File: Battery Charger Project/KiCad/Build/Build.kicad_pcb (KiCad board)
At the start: 2 copper layers, 135 x 107 mm, 63 parts, among them J1 726386-2, J10 726386-2, J11 726386-2, J2 726386-2, J3 726386-2, J4 Screw_Terminal_01x02, J5 726386-2, J6 726386-2, J7 726386-2, J8 Screw_Terminal_01x05, J9 726386-2, T1 Transformer_SP_1S, U1 LAUNCHXL-F28379D, U2 LNK6773K-TL, U3 MCS1801GS-25-P, U4 L4941BV

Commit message: More updates on PCB design
I forgot to push my changes for the last week, but I layed out the components and began routing traces and copper pours.
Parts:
- removed C11, C13, C14, C15, C16, C18, C19: C_Small, Capacitor_SMD:C_0805_2012Metric_Pad1.18x1.45mm_HandSolder
- removed C12: UHE1E102MHD6TO, footprints_C10:CAP_UAQ_12P5X20_NCH
- removed C17, C21: 0.1uF, Capacitor_SMD:C_0805_2012Metric_Pad1.18x1.45mm_HandSolder
- removed C20: ~, footprints_C20:CAP_WCAP-ATG5_05.0X11.0_WRE
- removed D2, D5: D_Zener, Diode_SMD:D_SMA-SMB_Universal_Handsoldering
- removed D3: US1M, Diode_SMD:D_SMA
- removed D4: STPS2H100U, footprints_SCHOTTKYDIODE:SMB_STM
- removed J10, J7, J9: 726386-2, KiCad:726386-2
- removed J11: 726386-2, Library:726386-2
- removed J8: Screw_Terminal_01x05, TerminalBlock_Phoenix:TerminalBlock_Phoenix_MPT-0,5-5-2.54_1x05_P2.54mm_Horizontal
- removed R10, R14, R15, R16, R17, R9: R_Small_US, Resistor_SMD:R_2010_5025Metric
- removed R11, R12, R19: R_Small_US, Resistor_SMD:R_0805_2012Metric
- removed R13: R_Small_US, Resistor_SMD:R_0805_2012Metric_Pad1.20x1.40mm_HandSolder
- removed R18, R20, R7: R_Small_US, Resistor_SMD:R_1206_3216Metric
- removed R8: R_Small_US, Resistor_SMD:R_1206_3216Metric_Pad1.30x1.75mm_HandSolder
- removed T1: Transformer_SP_1S, Library:Transformer_cust_v1
- removed U3: MCS1801GS-25-P, KiCadCS:SOIC127P600X175-8N
- removed U4: L4941BV, L4941BV:TO-220_STM
- C1: value UVR2G220MHD -> C_Small; footprint footprints_C1:CAP_UAQ_16X25_NCH -> Capacitor_SMD:C_0805_2012Metric_Pad1.18x1.45mm_HandSolder; moved to B.Cu
- C10, C3: value C_Small -> ~; footprint Capacitor_SMD:C_1206_3216Metric -> LGW2D561MELA30:CAP_A30_NCH; moved to F.Cu
- C2: footprint Capacitor_SMD:C_1206_3216Metric -> Capacitor_SMD:C_0805_2012Metric_Pad1.18x1.45mm_HandSolder; moved to B.Cu
- C4: value B32673P6225K000 -> C_Small; footprint KiCad_B326:B32673P__26.5_x_12_ -> Capacitor_SMD:C_0805_2012Metric_Pad1.18x1.45mm_HandSolder; moved to B.Cu
- C5, C6: moved to B.Cu
- C7: footprint footprints:CAP_C45_NCH -> EEU-FR1H100:CAP_PAN_5X11_PAN
- C8: value C_Small -> ~; footprint Capacitor_SMD:C_0805_2012Metric_Pad1.18x1.45mm_HandSolder -> LGW2D561MELA30:CAP_A30_NCH
- C9: value C_Small -> ~; footprint Capacitor_SMD:C_0805_2012Metric_Pad1.18x1.45mm_HandSolder -> LGW2D561MELA30:CAP_A30_NCH; moved to F.Cu
- D1: value US1M -> DNA40U2200GU; footprint Diode_SMD:D_SMA -> DPF30U200FC:DPF30U200FC; moved to F.Cu
- J1: value 726386-2 -> Screw_Terminal_01x03; footprint KiCad:726386-2 -> 284391-3:CONN3_284391-3_TEC
- J2: value 726386-2 -> Screw_Terminal_01x02; footprint KiCad:726386-2 -> 284391-2:CONN2_284391-2_TEC
- J3: value 726386-2 -> Screw_Terminal_01x03; footprint KiCad:726386-2 -> 277-1578-ND:CONN_1935174_PXC
- J4: value Screw_Terminal_01x02 -> 726386-2; footprint TerminalBlock:TerminalBlock_bornier-2_P5.08mm -> 284391-2:CONN2_284391-2_TEC
- J5, J6: footprint KiCad:726386-2 -> 284391-2:CONN2_284391-2_TEC
- L1: footprint Library:inductor_customized_v1 -> LC200-0185:LC200-0185
- R1: value R_US -> 300K; moved to B.Cu
- R2: value R_US -> 6490; moved to B.Cu
- R3: value R_US -> 36; moved to B.Cu
- R4: value R_US -> 5K; moved to B.Cu
- R5: value R_Small_US -> 680; footprint Resistor_SMD:R_1206_3216Metric -> Resistor_SMD:R_2010_5025Metric
- R6: value R_Small_US -> 680; moved to B.Cu
- U1: footprint Library:MOD_LAUNCHXL-F28379D_v2 -> LAUNCHXL-F28379D:LAUNCHXL-F28379D
- U2: value LNK6773K-TL -> TMCS1133C3A; footprint KiCad2:LNK6773KTL -> TMCS1133C5AQDVGR:TMCS1133C5AQDVGR
- moved J4 136.4 mm to (213.1, 131.4), turned to -90 degrees
- moved J3 124.3 mm to (89.9, 131.9), turned to -90 degrees
- moved D1 115.8 mm to (99.5, 134.9), turned to 180 degrees
- moved J5 114.3 mm to (213.9, 114.4), turned to 90 degrees
- moved C9 109.6 mm to (194.6, 127.7), turned to -90 degrees
- moved C4 86.2 mm to (178.3, 79.7)
- moved R5 71.4 mm to (130.6, 113.6), turned to 90 degrees
- moved R4 69.0 mm to (140.2, 113.6)
- moved C3 68.7 mm to (168.4, 127.6)
- moved U1 67.9 mm to (216.5, 31.7), turned to 180 degrees
- moved C10 67.8 mm to (142.2, 127.6), turned to -90 degrees
- moved R3 65.2 mm to (200.7, 137.5), turned to 180 degrees
- moved R1 65.0 mm to (200.7, 127.9), turned to 0 degrees
- moved R2 65.0 mm to (202.3, 132.7)
- moved C2 64.9 mm to (209.5, 53.0), turned to 90 degrees
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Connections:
- C1 pad 1: Net-(D1-K) -> PWMA
- C10 pad 1: Net-(C10-Pad1) -> VHV
- C10 pad 2: 12V -> GND
- C2 pad 1: Net-(U2-PD) -> 5V
- C3 pad 1: Net-(C3-Pad1) -> VHV
- C3 pad 2: Net-(D2-K) -> GND
- C4 pad 1: GND -> VHV_S
- C4 pad 2: Net-(C4-Pad2) -> GND
- C5 pad 1: Net-(U2-CP) -> Vo_S
- C5 pad 2: Net-(C5-Pad2) -> GND
- C6 pad 1: Net-(U2-BP) -> Io_S
- C7 pad 1: Net-(U3-IP+_1) -> Net-(U2-IN+)
- C8 pad 1: Net-(U2-CP) -> VHV
- C9 pad 1: PWMA -> VHV
- D1 pad 1: Net-(D1-K) -> VHV
- D1 pad 2: VHV -> GND
- J1 pad 1: VHV -> GND
- J1 pad 2: VHV -> PWMA
- J2 pad 1: GND -> 5V
- J3 pad 1: unconnected-(J3-Pad1) -> /A
- J3 pad 2: unconnected-(J3-Pad1) -> /B
- J4 pad 1: 12V -> VHV
- J6 pad 1: Net-(C4-Pad2) -> GND
- J6 pad 2: Net-(C4-Pad2) -> Vo
- L1 pad 2: Net-(U3-IP+_1) -> Net-(U2-IN+)
- R1 pad 2: Net-(R1-Pad2) -> VHV_S
- R2 pad 1: Net-(R1-Pad2) -> VHV_S
- R3 pad 2: VHV1 -> GND
- R4 pad 1: VHV1 -> Net-(U2-IN+)
- R4 pad 2: GND -> Vo_S
- R5 pad 1: Net-(D1-K) -> Net-(R5-Pad1)
- R5 pad 2: Net-(D2-A) -> GND
- R6 pad 1: Net-(U2-PD) -> Vo_S
- R6 pad 2: GND -> Net-(R5-Pad1)
- U1 pad J3_10: Net-(U1C-ADCINA0/ANALOGIN(DACA)) -> Io_S
- U1 pad J3_4: VHV1 -> VHV_S
- U1 pad J3_7: Board Temp -> unconnected-(U1C-ADCINC2/ANALOGIN-PadJ3_7)
- U1 pad J3_8: Vo -> Vo_S
- U1 pad J4_9: PWMB -> unconnected-(U1D-GPIO1/PWMOUT1B-PadJ4_9)
- U2 pad 1: Net-(U2-PD) -> Net-(U2-IN+)
- U2 pad 10: GND -> (no net)
- U2 pad 2: Net-(U2-FB) -> Vo
- U2 pad 3: Net-(U2-CP) -> GND
- U2 pad 4: Net-(U2-BP) -> (no net)
- U2 pad 6: Net-(D3-A) -> Io_S
- U2 pad 7: GND -> (no net)
- U2 pad 8: GND -> (no net)
- U2 pad 9: GND -> +5V
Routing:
- net GND: track 624.9 -> 3.86 mm, vias 2 -> 0
- net 5V: track 260.0 -> 0.00 mm, vias 3 -> 0
- net Vo: track 162.5 -> 0.00 mm, vias 1 -> 0
- net Ibatt: track 145.5 -> 0.00 mm
- net VHV1: track 115.5 -> 0.00 mm
- net Net-(U3-IP+_1): track 60.1 -> 0.00 mm
- net Board Temp: track 59.9 -> 0.00 mm, vias 2 -> 0
- net Net-(C4-Pad2): track 53.3 -> 0.00 mm
- net PWMA: track 52.2 -> 0.00 mm
- net 12V: track 47.9 -> 0.00 mm
- net PWMB: track 46.6 -> 0.00 mm
- net Net-(U2-BP): track 41.8 -> 0.00 mm, vias 2 -> 0
- net Net-(U2-FB): track 35.3 -> 0.00 mm, vias 2 -> 0
- net VHV: track 37.2 -> 3.88 mm
- net Net-(J5-Pad1): track 26.8 -> 0.00 mm
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- added copper zone on B.Cu, net /A
- added copper zone on F.Cu, net /A
- added copper zone on B.Cu, net /B
- added copper zone on F.Cu, net /B
- added copper zone on B.Cu, net /C
- added copper zone on F.Cu, net /C
- added copper zone on B.Cu, net Net-(U2-IN+)
- added copper zone on F.Cu, net Net-(U2-IN+)
- added copper zone on B.Cu, net VHV
- added copper zone on F.Cu, net VHV
- added copper zone on B.Cu, net Vo
- removed copper zone on B.Cu, net IP-
- removed copper zone on B.Cu, net Net-(J5-Pad1)
- removed copper zone on B.Cu, net Net-(U3-IP+_1)
- removed copper zone on F.Cu, net Net-(U3-IP+_1)
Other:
- board size 135 x 107 mm -> 135 x 115 mm

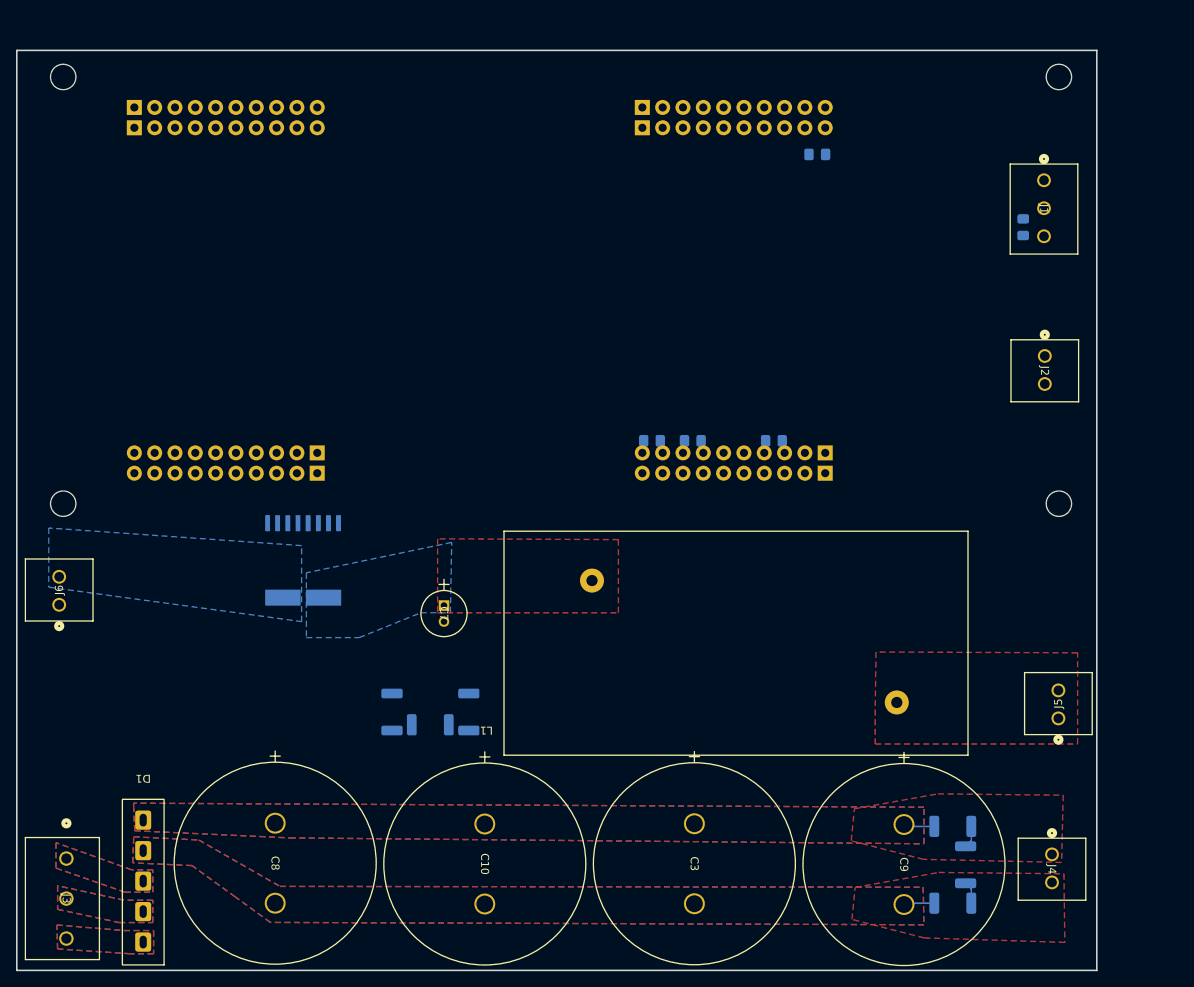
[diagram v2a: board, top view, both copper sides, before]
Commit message: PCB updates
Dr. Mcintyre suggested using large pours for the high voltage and gnd planes. He also asked me to implement design constraints. The main concern is the distance between the high DC bus and gnd near the rectifier.
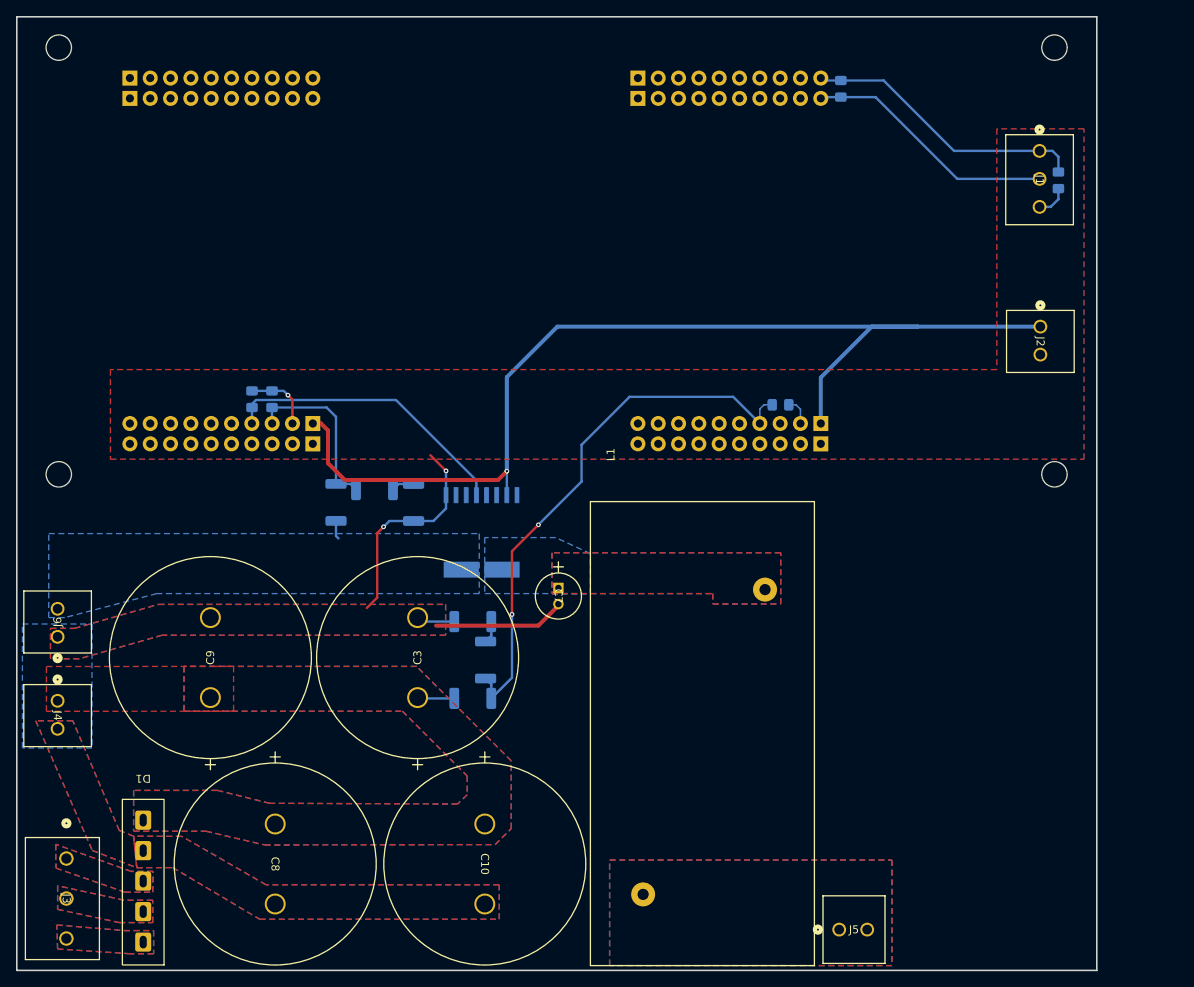
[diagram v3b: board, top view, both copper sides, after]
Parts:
- moved J4 125.8 mm to (88.8, 112.2)
- moved C9 88.1 mm to (107.9, 111.8), turned to 90 degrees
- moved R3 69.6 mm to (140.7, 102.3)
- moved R2 65.2 mm to (142.3, 107.1), turned to 90 degrees
- moved R1 62.1 mm to (140.7, 111.9)
- moved C5 52.9 mm to (115.6, 74.5), turned to 90 degrees
- moved C6 50.3 mm to (113.1, 74.5), turned to 90 degrees
- moved J5 38.0 mm to (186.5, 140.8), turned to 0 degrees
- moved C3 38.0 mm to (133.8, 111.8), turned to 90 degrees
- moved R4 31.0 mm to (123.6, 87.4), turned to 90 degrees
- moved R6 30.2 mm to (128.4, 85.8), turned to 0 degrees
- moved R5 26.3 mm to (133.3, 87.4), turned to -90 degrees
- moved U2 22.6 mm to (141.8, 91.1)
- moved L1 15.5 mm to (162.0, 98.3), turned to -90 degrees
- moved C7 14.5 mm to (151.4, 98.1)
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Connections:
- R4 pad 1: Net-(U2-IN+) -> Vo
- U1 pad J3_10: Io_S -> unconnected-(U1C-ADCINA0/ANALOGIN(DACA)-PadJ3_10)
- U1 pad J3_8: Vo_S -> unconnected-(U1C-ADCINB2/ANALOGIN-PadJ3_8)
- U1 pad J7_3: unconnected-(U1G-ADCIN15/ANALOGIN-PadJ7_3) -> Vo_S
- U1 pad J7_4: unconnected-(U1G-ADCINC5/ANALOGIN-PadJ7_4) -> Io_S
- U2 pad 9: +5V -> 5V
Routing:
- net 5V: track 0.00 -> 138.7 mm, vias 0 -> 1
- net GND: track 3.86 -> 96.8 mm, vias 0 -> 3
- net VHV_S: track 2.78 -> 69.0 mm, vias 0 -> 2
- net Io_S: track 0.00 -> 36.7 mm
- net PWMA: track 0.00 -> 31.6 mm
- net Vo_S: track 0.00 -> 21.7 mm
- net Net-(R5-Pad1): track 0.00 -> 2.86 mm
- net Vo: track 0.00 -> 2.31 mm
- net VHV: track 3.88 -> 5.59 mm
- added copper zone on B.Cu, net Net-(J5-Pad1)
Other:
- board size 135 x 115 mm -> 135 x 119.2 mm

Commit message: PCB updates
Added pours and net class clearances
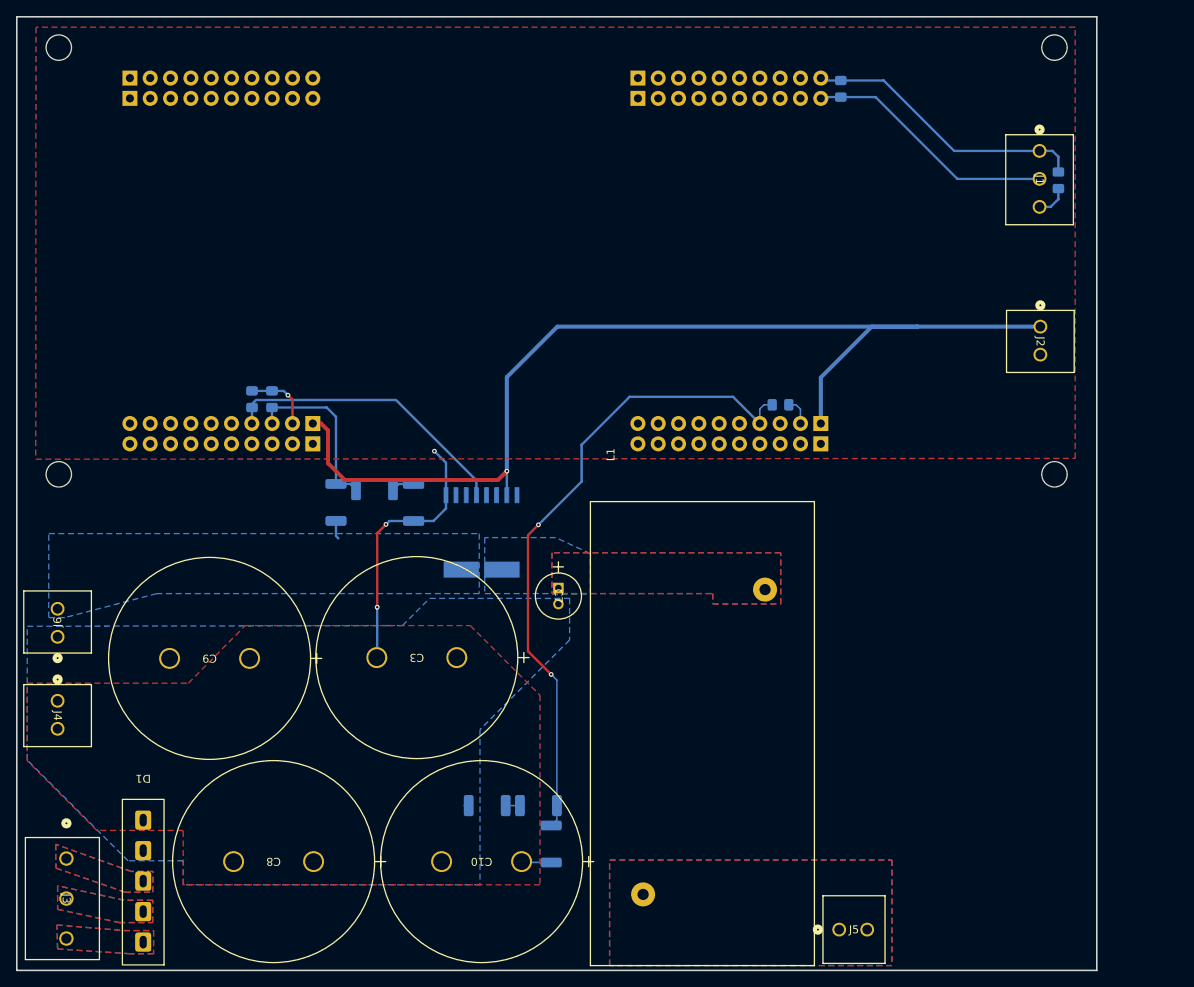
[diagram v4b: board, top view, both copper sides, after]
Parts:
- moved R3 23.1 mm to (142.5, 125.3)
- moved R1 20.7 mm to (150.5, 130.1), turned to 90 degrees
- moved R2 19.4 mm to (148.9, 125.3), turned to 180 degrees
- moved C3 7.00 mm to (138.7, 106.8), turned to 180 degrees
- moved C9 6.93 mm to (112.8, 106.9), turned to 180 degrees
- moved C8 6.72 mm to (120.8, 132.3), turned to 180 degrees
- moved C10 6.58 mm to (146.8, 132.3), turned to 180 degrees
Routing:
- net GND: track 96.8 -> 81.8 mm, vias 3 -> 4
- net VHV_S: track 69.0 -> 82.0 mm
- net VHV: track 5.59 -> 3.71 mm
- net Net-(R2-Pad2): track 2.78 -> 1.78 mm
- removed copper zone on B.Cu, net VHV
